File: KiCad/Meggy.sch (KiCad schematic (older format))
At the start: 15 parts, among them J1 USB_B_Micro, J2 Conn_01x03, U1 ROM-socket-42pin, U2 AT90USB1286-MU, U3 M29F160F, X1 Standard_Clock_Oscillators_XT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

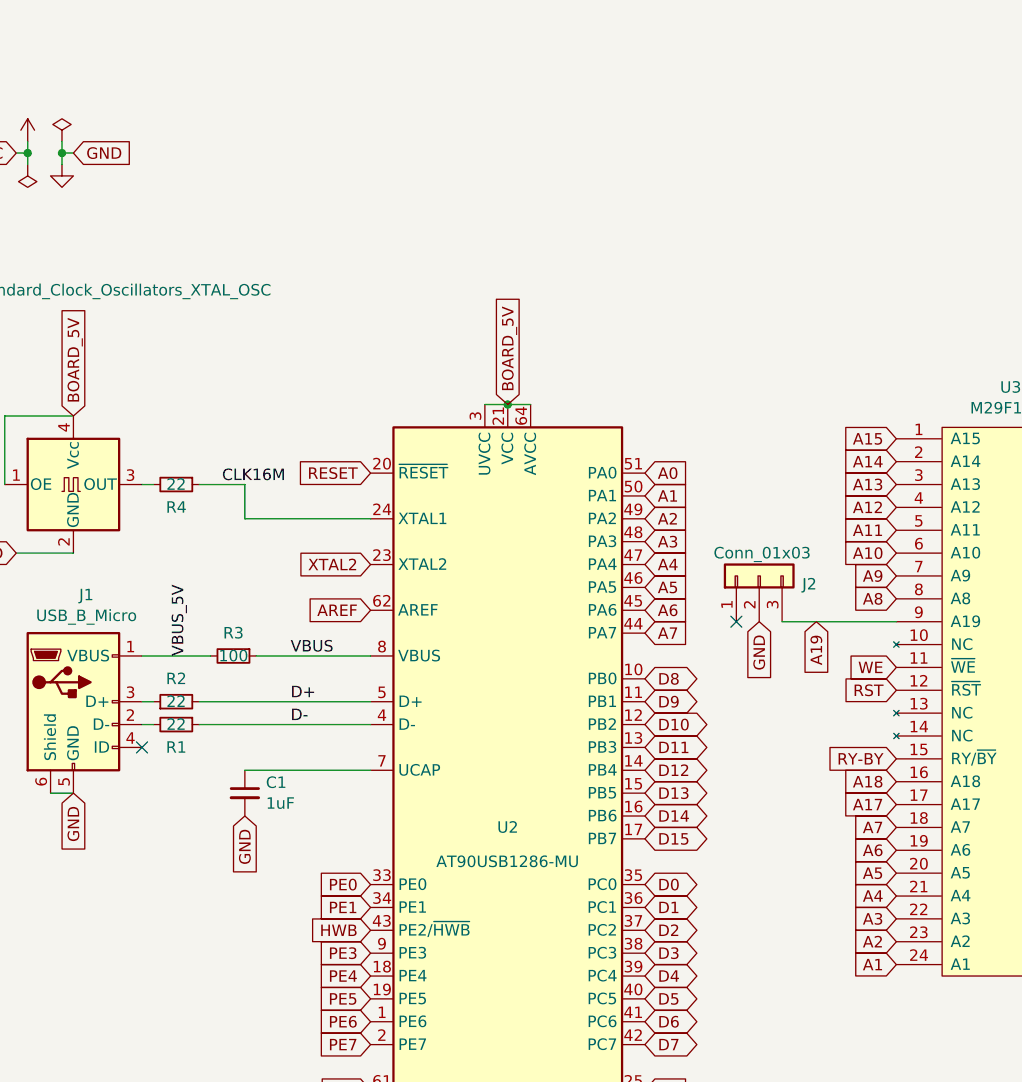
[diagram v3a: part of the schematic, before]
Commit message: Added Q1 and Q2 MOSFETs, changed footprint on CLK16M resistor and routed RST and WE signals
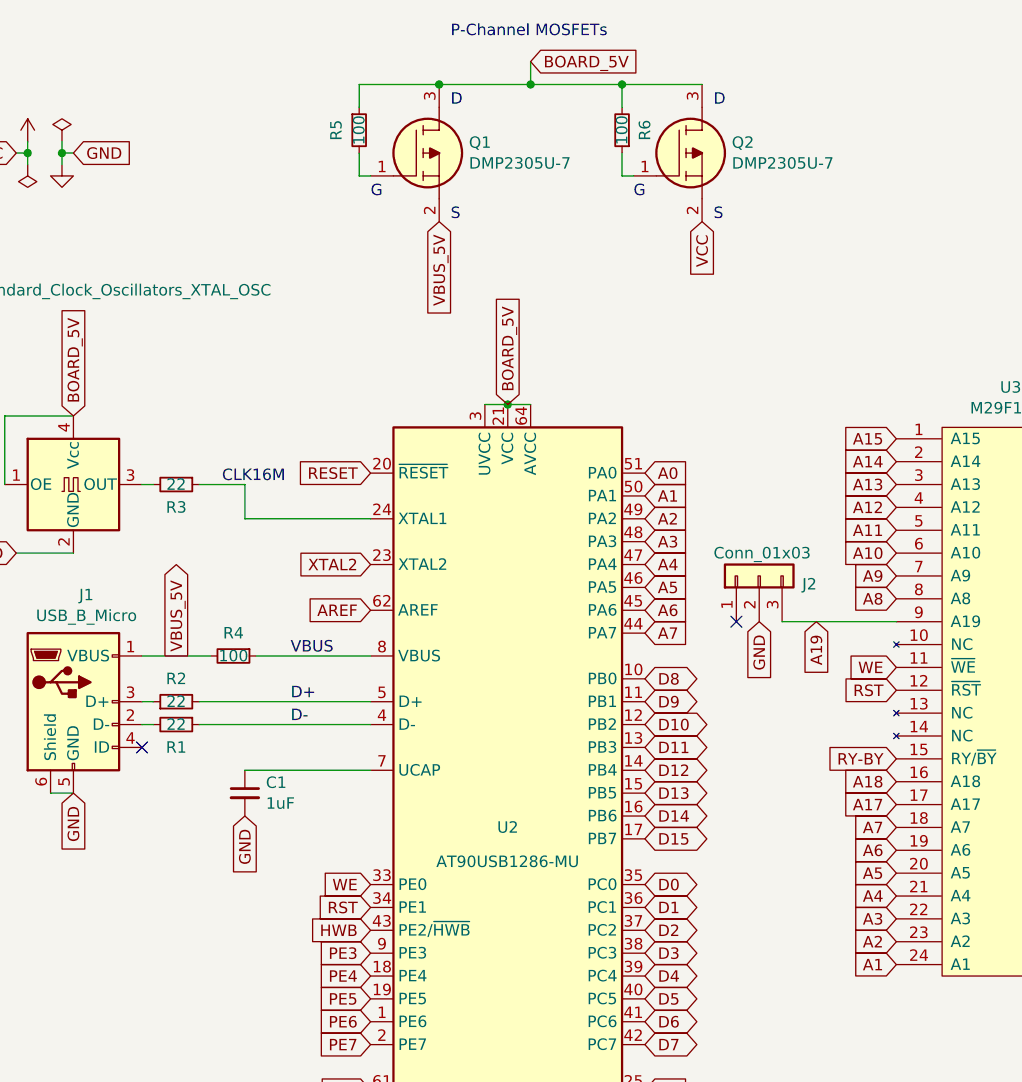
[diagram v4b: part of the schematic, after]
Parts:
- added Q1, Q2: DMP2305U-7, Package_TO_SOT_SMD:SOT-23, symbol Meggy:DMP2305U-7
- added R5, R6: 100, Resistor_SMD:R_0603_1608Metric_Pad0.98x0.95mm_HandSolder, symbol Device:R_Small
- R3: renamed from R4; footprint Resistor_SMD:R_0603_1608Metric_Pad0.98x0.95mm_HandSolder -> Resistor_SMD:R_0603_1608Metric
- renumbered R3 to R4
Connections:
- net PE0 is gone; now on net WE: U2.33 (PE0)
- net PE1 is gone; now on net RST: U2.34 (PE1)
- net BOARD_5V: now also Q1.3, Q2.3, R5.1, R6.2
- net VBUS_5V: now also Q1.2
- net VCC: now also Q2.2
- new net: Q1.1, R5.2
- new net: Q2.1, R6.1
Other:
- note added: "D"
- note added: "G"
- note added: "P-Channel MOSFETs"
- note added: "S"
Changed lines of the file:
@@
 	1    0    0    -1
 $EndComp
-Text Label 1750 3350 1    50   ~ 0
-VBUS_5V
 Text Label 2200 3350 0    50   ~ 0
 VBUS
@@
 	1550 3650 1600 3650
 $Comp
-L Device:R_Small R3
+L Device:R_Small R4
 U 1 1 68CDBE7C
 P 1950 3350
-F 0 "R3" V 1850 3350 50  0000 C CNN
+F 0 "R4" V 1850 3350 50  0000 C CNN
 F 1 "100" V 1950 3350 50  0000 C CNN
 F 2 "Resistor_SMD:R_0603_1608Metric_Pad0.98x0.95mm_HandSolder" H 1950 3350 50  0001 C CNN
@@
 Text GLabel 2550 4550 0    50   Input ~ 0
 HWB
-Text GLabel 2550 4350 0    50   Input ~ 0
-PE0
-Text GLabel 2550 4450 0    50   Input ~ 0
-PE1
 Text GLabel 2550 4650 0    50   Input ~ 0
 PE3
@@
 	1000 2900 1250 2900
 $Comp
-L Device:R_Small R4
+L Device:R_Small R3
 U 1 1 68CFCC9A
 P 1700 2600
-F 0 "R4" V 1800 2600 50  0000 C CNN
+F 0 "R3" V 1800 2600 50  0000 C CNN
 F 1 "22" V 1700 2600 50  0000 C CNN
-F 2 "Resistor_SMD:R_0603_1608Metric_Pad0.98x0.95mm_HandSolder" H 1700 2600 50  0001 C CNN
+F 2 "Resistor_SMD:R_0603_1608Metric" H 1700 2600 50  0001 C CNN
 F 3 "~" H 1700 2600 50  0001 C CNN
 	1    1700 2600
@@
 	6600 5650 6600 5600
 Connection ~ 6200 5650
+Text Notes 2550 1350 0    50   ~ 0
+G
+Text Notes 2900 950  0    50   ~ 0
+D
+Text Notes 2900 1450 0    50   ~ 0
+S
+Text Notes 2900 650  0    50   ~ 0
+P-Channel MOSFETs
+Text GLabel 3250 750  2    50   Input ~ 0
+BOARD_5V
+$Comp
+L Meggy:DMP2305U-7 Q1
+U 1 1 68D8212F
+P 2550 1250
+F 0 "Q1" H 2980 1396 50  0000 L CNN
+F 1 "DMP2305U-7" H 2980 1305 50  0000 L CNN
+F 2 "Package_TO_SOT_SMD:SOT-23" H 3000 1200 50  0001 L CNN
+F 3 "https://www.diodes.com//assets/Datasheets/DMP2305U.pdf" H 3000 1100 50  0001 L CNN
+	1    2550 1250
+	1    0    0    -1
+$EndComp
+Text Notes 3700 1350 0    50   ~ 0
+G
+Text Notes 4050 950  0    50   ~ 0
+D
+Text Notes 4050 1450 0    50   ~ 0
+S
+$Comp
+L Meggy:DMP2305U-7 Q2
+U 1 1 68D926EB
+P 3700 1250
+F 0 "Q2" H 4130 1396 50  0000 L CNN
+F 1 "DMP2305U-7" H 4130 1305 50  0000 L CNN
+F 2 "Package_TO_SOT_SMD:SOT-23" H 4150 1200 50  0001 L CNN
+F 3 "https://www.diodes.com//assets/Datasheets/DMP2305U.pdf" H 4150 1100 50  0001 L CNN
+	1    3700 1250
+	1    0    0    -1
+$EndComp
+Text GLabel 1700 3350 1    50   Output ~ 0
+VBUS_5V
+Text GLabel 2850 1450 3    50   Input ~ 0
+VBUS_5V
+Text GLabel 4000 1450 3    50   Input ~ 0
+VCC
+$Comp
+L Device:R_Small R6
+U 1 1 68D97863
+P 3650 1050
+F 0 "R6" V 3550 1050 50  0000 C CNN
+F 1 "100" V 3650 1050 50  0000 C CNN
+F 2 "Resistor_SMD:R_0603_1608Metric_Pad0.98x0.95mm_HandSolder" H 3650 1050 50  0001 C CNN
+F 3 "~" H 3650 1050 50  0001 C CNN
+	1    3650 1050
+	-1   0    0    1
+$EndComp
+$Comp
+L Device:R_Small R5
+U 1 1 68D98E8C
+P 2500 1050
+F 0 "R5" V 2400 1050 50  0000 C CNN
+F 1 "100" V 2500 1050 50  0000 C CNN
+F 2 "Resistor_SMD:R_0603_1608Metric_Pad0.98x0.95mm_HandSolder" H 2500 1050 50  0001 C CNN
+F 3 "~" H 2500 1050 50  0001 C CNN
+	1    2500 1050
+	1    0    0    -1
+$EndComp
+Wire Wire Line
+	2550 1250 2500 1250
+Wire Wire Line
+	2500 1250 2500 1150
+Wire Wire Line
+	3700 1250 3650 1250
+Wire Wire Line
+	3650 1250 3650 1150
+Wire Wire Line
+	2500 950  2500 850
+Wire Wire Line
+	2500 850  2850 850
+Connection ~ 2850 850
+Wire Wire Line
+	3650 950  3650 850
+Connection ~ 3650 850
+Wire Wire Line
+	3650 850  4000 850
+Wire Wire Line
+	3250 750  3250 850
+Wire Wire Line
+	3250 850  3650 850
+Wire Wire Line
+	2850 850  3250 850
+Connection ~ 3250 850
+Text GLabel 2550 4450 0    50   Input ~ 0
+RST
+Text GLabel 2550 4350 0    50   Input ~ 0
+WE
 $EndSCHEMATC

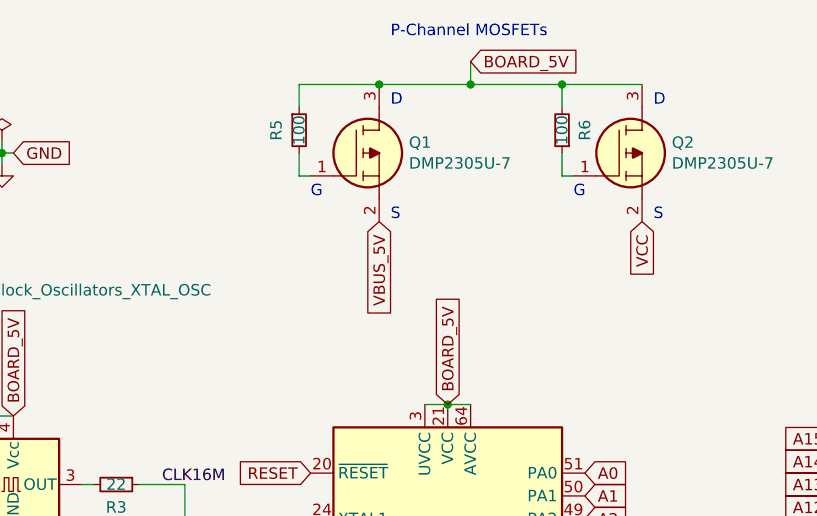
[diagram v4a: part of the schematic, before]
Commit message: Removed R5,R6 and added D1,D2 changing the 5V Power Protection & ORing Circuit
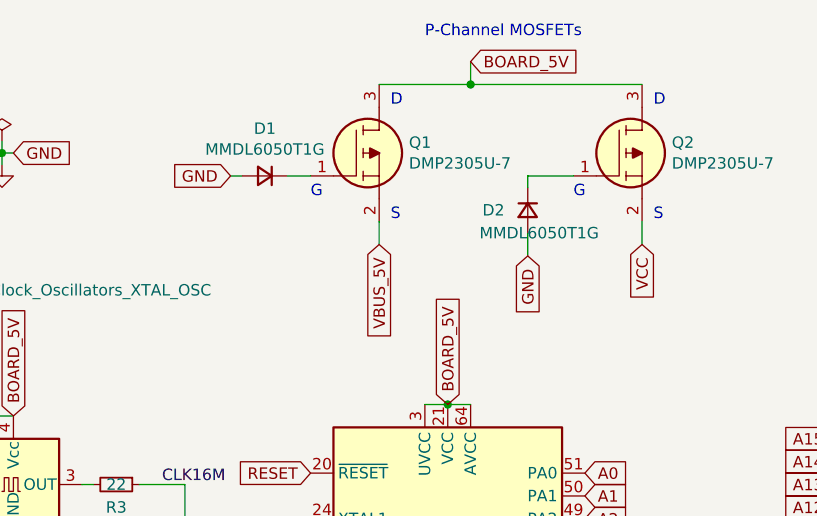
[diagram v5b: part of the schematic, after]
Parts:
- removed R5, R6: 100, Resistor_SMD:R_0603_1608Metric_Pad0.98x0.95mm_HandSolder, symbol Device:R_Small
- added D1, D2: MMDL6050T1G, Meggy:D_0603_1608Metric_Pad_0.975x0.95mm_HandSolder, symbol Device:D_Small
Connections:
- net GND: now also D1.2 (A), D2.2 (A)
- net at Q1.1: now also D1.1 (K)
- net at Q2.1: now also D2.1 (K)
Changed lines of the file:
@@
 Text Notes 2900 1450 0    50   ~ 0
 S
-Text Notes 2900 650  0    50   ~ 0
+Text Notes 3050 650  0    50   ~ 0
 P-Channel MOSFETs
 Text GLabel 3250 750  2    50   Input ~ 0
@@
 Text GLabel 1700 3350 1    50   Output ~ 0
 VBUS_5V
-Text GLabel 2850 1450 3    50   Input ~ 0
+Text GLabel 2850 1550 3    50   Input ~ 0
 VBUS_5V
-Text GLabel 4000 1450 3    50   Input ~ 0
+Text GLabel 4000 1550 3    50   Input ~ 0
 VCC
-$Comp
-L Device:R_Small R6
-U 1 1 68D97863
-P 3650 1050
-F 0 "R6" V 3550 1050 50  0000 C CNN
-F 1 "100" V 3650 1050 50  0000 C CNN
-F 2 "Resistor_SMD:R_0603_1608Metric_Pad0.98x0.95mm_HandSolder" H 3650 1050 50  0001 C CNN
-F 3 "~" H 3650 1050 50  0001 C CNN
-	1    3650 1050
-	-1   0    0    1
-$EndComp
-$Comp
-L Device:R_Small R5
-U 1 1 68D98E8C
-P 2500 1050
-F 0 "R5" V 2400 1050 50  0000 C CNN
-F 1 "100" V 2500 1050 50  0000 C CNN
-F 2 "Resistor_SMD:R_0603_1608Metric_Pad0.98x0.95mm_HandSolder" H 2500 1050 50  0001 C CNN
-F 3 "~" H 2500 1050 50  0001 C CNN
-	1    2500 1050
-	1    0    0    -1
-$EndComp
-Wire Wire Line
-	2550 1250 2500 1250
-Wire Wire Line
-	2500 1250 2500 1150
-Wire Wire Line
-	3700 1250 3650 1250
-Wire Wire Line
-	3650 1250 3650 1150
-Wire Wire Line
-	2500 950  2500 850
-Wire Wire Line
-	2500 850  2850 850
-Connection ~ 2850 850
-Wire Wire Line
-	3650 950  3650 850
-Connection ~ 3650 850
-Wire Wire Line
-	3650 850  4000 850
 Wire Wire Line
 	3250 750  3250 850
-Wire Wire Line
-	3250 850  3650 850
 Wire Wire Line
 	2850 850  3250 850
@@
 Text GLabel 2550 4350 0    50   Input ~ 0
 WE
+Wire Wire Line
+	2850 1450 2850 1550
+Wire Wire Line
+	4000 1450 4000 1550
+Text GLabel 2200 1250 0    50   Input ~ 0
+GND
+Wire Wire Line
+	2250 1250 2200 1250
+Text GLabel 3500 1600 3    50   Input ~ 0
+GND
+Wire Wire Line
+	3500 1250 3500 1300
+Wire Wire Line
+	3250 850  4000 850
+$Comp
+L Device:D_Small D1
+U 1 1 68E1A907
+P 2350 1250
+F 0 "D1" H 2350 1043 50  0000 C CNN
+F 1 "MMDL6050T1G" H 2350 1134 50  0000 C CNN
+F 2 "Meggy:D_0603_1608Metric_Pad_0.975x0.95mm_HandSolder" V 2350 1250 50  0001 C CNN
+F 3 "~" V 2350 1250 50  0001 C CNN
+	1    2350 1250
+	-1   0    0    1
+$EndComp
+Wire Wire Line
+	2450 1250 2550 1250
+Wire Wire Line
+	3500 1250 3700 1250
+$Comp
+L Device:D_Small D2
+U 1 1 68E38814
+P 3500 1400
+F 0 "D2" V 3500 1250 50  0000 C CNN
+F 1 "MMDL6050T1G" V 3600 1450 50  0000 C CNN
+F 2 "Meggy:D_0603_1608Metric_Pad_0.975x0.95mm_HandSolder" V 3500 1400 50  0001 C CNN
+F 3 "~" V 3500 1400 50  0001 C CNN
+	1    3500 1400
+	0    1    1    0
+$EndComp
+Wire Wire Line
+	3500 1500 3500 1600
 $EndSCHEMATC
